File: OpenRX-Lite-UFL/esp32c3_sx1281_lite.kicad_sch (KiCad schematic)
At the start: 39 parts, among them U1 ESP32-C3FH4, U2 TLV75533PDQNR, U3 SX1281IMLTRT, X1 CJ17-400001010B20

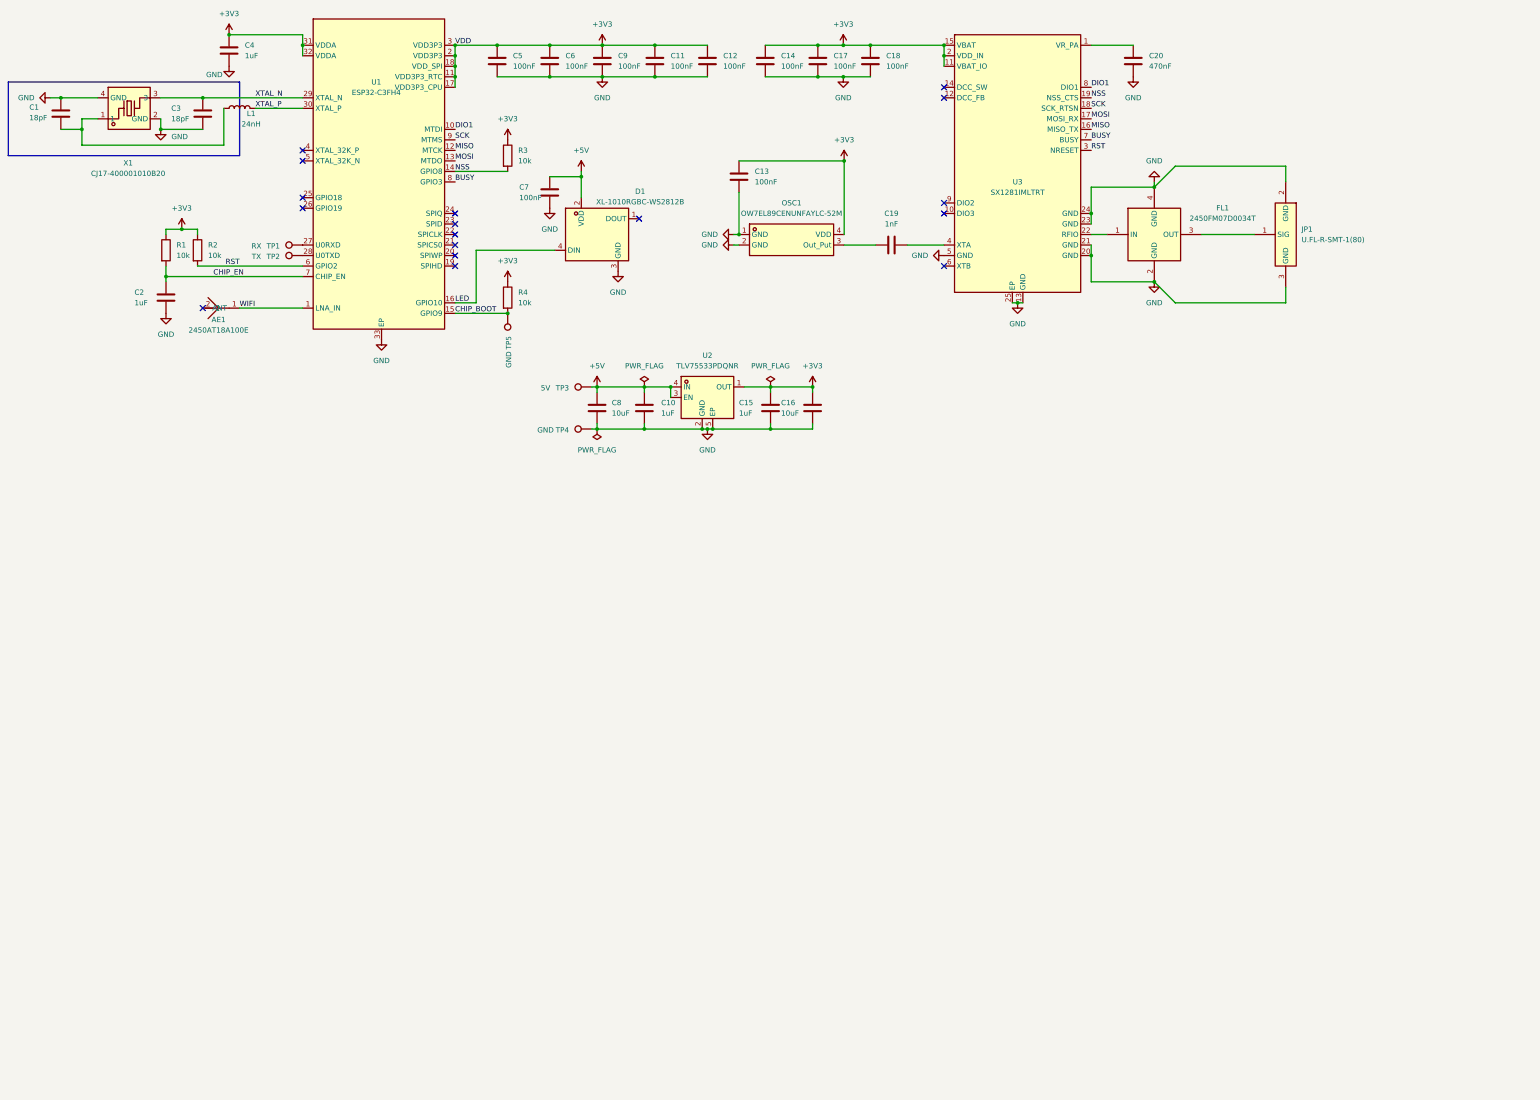
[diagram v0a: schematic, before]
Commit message: OpenRX Lite (UFL + molex)
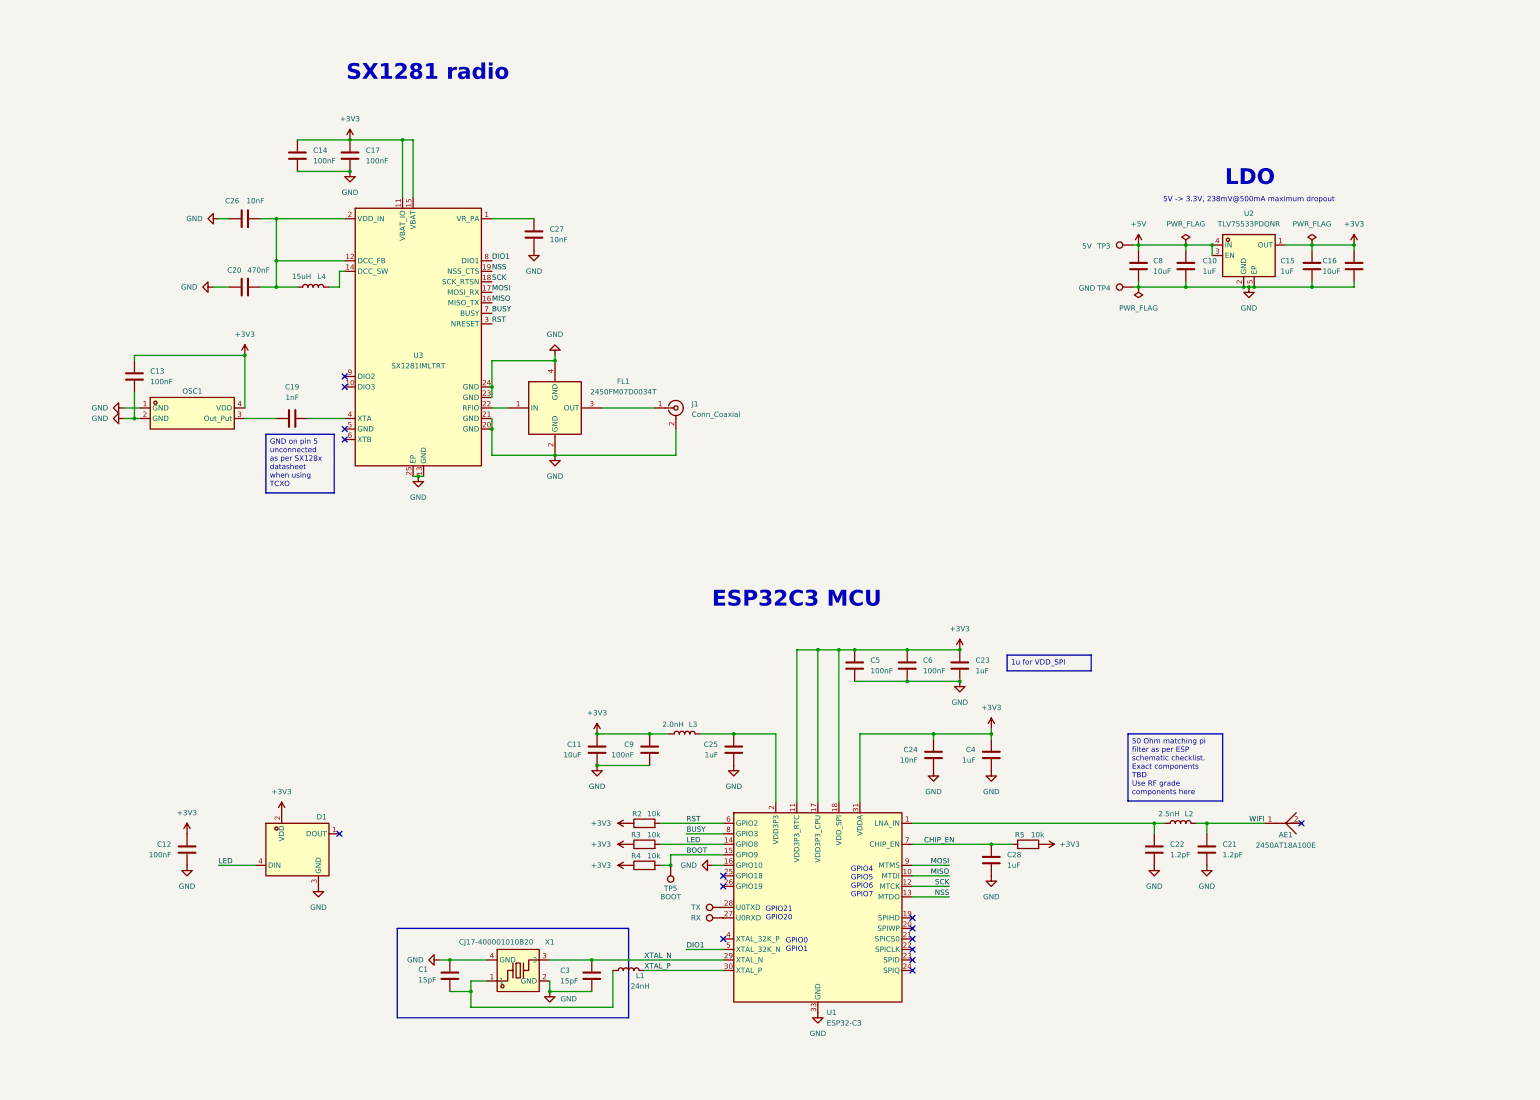
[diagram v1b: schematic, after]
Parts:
- removed C18, C7: 100nF, Capacitor_SMD:C_0201_0603Metric, symbol Device:C
- removed C2: 1uF, Capacitor_SMD:C_0201_0603Metric, symbol Device:C
- removed JP1: U.FL-R-SMT-1(80), OpenRX-Shared:RF-SMD_FRF05002-JSS103M, symbol OpenRX-Shared:U.FL-R-SMT-1(80)
- removed R1: 10k, Resistor_SMD:R_0201_0603Metric, symbol Device:R
- removed U1: ESP32-C3FH4, OpenRX-Shared:QFN-32_L5.0-W5.0-P0.50-TL-EP3.7, symbol OpenRX-Shared:ESP32-C3FH4
- added C21, C22: 1.2pF, Capacitor_SMD:C_0201_0603Metric, symbol Device:C
- added C23, C25, C28: 1uF, Capacitor_SMD:C_0201_0603Metric, symbol Device:C
- added C24, C26, C27: 10nF, Capacitor_SMD:C_0201_0603Metric, symbol Device:C
- added J1: Conn_Coaxial, Connector_Coaxial:U.FL_Hirose_U.FL-R-SMT-1_Vertical, symbol Connector:Conn_Coaxial
- added L2: 2.5nH, Inductor_SMD:L_0201_0603Metric, symbol Device:L
- added L3: 2.0nH, Inductor_SMD:L_0201_0603Metric, symbol Device:L
- added L4: 15uH, Inductor_SMD:L_0805_2012Metric, symbol Device:L
- added R5: 10k, Resistor_SMD:R_0201_0603Metric, symbol Device:R
- added U1: ESP32-C3, Package_DFN_QFN:QFN-32-1EP_5x5mm_P0.5mm_EP3.7x3.7mm, symbol MCU_Espressif:ESP32-C3
- C1, C3: value 18pF -> 15pF; LCSC C62164 -> C85891; LCSC Part C62164 -> C85891
- C11: value 100nF -> 10uF; footprint Capacitor_SMD:C_0201_0603Metric -> Capacitor_SMD:C_0402_1005Metric; LCSC C76939 -> C76991; LCSC Part C76939 -> (none)
- D1: LCSC C5349953 -> (none)
- TP5: value GND -> BOOT
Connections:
- net +3V3: now also D1.2 (VDD), C23.1, C24.1, L3.2, R5.2, U1.11 (VDD3P3_RTC), U1.17 (VDD3P3_CPU), U1.18 (VDD_SPI), U1.31 (VDDA), U1.32 (VDDA); no longer U3.2 (VDD_IN)
- net +5V: no longer D1.2 (VDD)
- net BUSY: now also U1.8 (GPIO3)
- net CHIP_EN: now also C28.1, R5.1, U1.7 (CHIP_EN)
- net DIO1: now also U1.5 (XTAL_32K_N)
- net GND: now also C20.1, C21.2, C22.2, C23.2, C24.2, C25.2, C26.1, C27.2, C28.2, J1.2 (Ext), U1.16 (GPIO10), U1.33 (GND); no longer C20.2, U3.5 (GND)
- net LED: now also R3.2, U1.14 (GPIO8)
- net MISO: now also U1.10 (MTDI)
- net MOSI: now also U1.9 (MTMS)
- net NSS: now also U1.13 (MTDO); no longer R3.2
- net RST: now also U1.6 (GPIO2)
- net SCK: now also U1.12 (MTCK)
- net WIFI: now also C21.1, L2.1
- net XTAL_N: now also U1.29 (XTAL_N)
- net XTAL_P: now also U1.30 (XTAL_P)
- net at TP1.1: now also U1.27 (U0RXD)
- net at TP2.1: now also U1.28 (U0TXD)
- net at FL1.3 (OUT): now also J1.1 (In)
- net at U3.1 (VR_PA): now also C27.1; no longer C20.1
- net at U3.12 (DCC_FB): now also C20.2, U3.2 (VDD_IN), C26.2, L4.1
- net at U3.14 (DCC_SW): now also L4.2
- net CHIP_BOOT renamed BOOT
- net BOOT: now also U1.15 (GPIO9)
- new net: C25.1, L3.1, U1.2 (VDD3P3), U1.3 (VDD3P3)
- new net: C22.1, L2.2, U1.1 (LNA_IN)
- no-connect marks 17 -> 15
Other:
- note added: "5V -> 3.3V, 238mV@500mA maximum dropout"
- note added: "ESP32C3 MCU"
- note added: "GPIO0 GPIO1"
- note added: "GPIO21 GPIO20"
- note added: "GPIO4 GPIO5 GPIO6 GPIO7"
- note added: "LDO"
- note added: "SX1281 radio"
- moved on the sheet: C10, C13, C15, C16, C19, C8, FL1, OSC1, TP3, TP4, U2, U3

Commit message: annotate
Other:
- note added: "07/06/2026"
- note added: "1"
- note added: "SX1281 + ESP32-C3 + LDO + RGB LED (full ELRS)"
- moved on the sheet: AE1, C1, C10, C11, C12, C15, C16, C21, C22, C23, C24, C25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
